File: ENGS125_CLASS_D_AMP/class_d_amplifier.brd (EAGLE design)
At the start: 100 x 80 mm, 24 parts, among them J1 BANANA_JACK_CT3151, J2 BANANA_JACK_CT3151, J3 BANANA_JACK_CT3151, J4 BANANA_JACK_CT3151, J5 BANANA_JACK_CT3151, J6 BANANA_JACK_CT3151, M1 BSC050NE2LSATMA1, M2 BSC050NE2LSATMA1, U1 LTC6992TSOT-23, U2 LTC4449

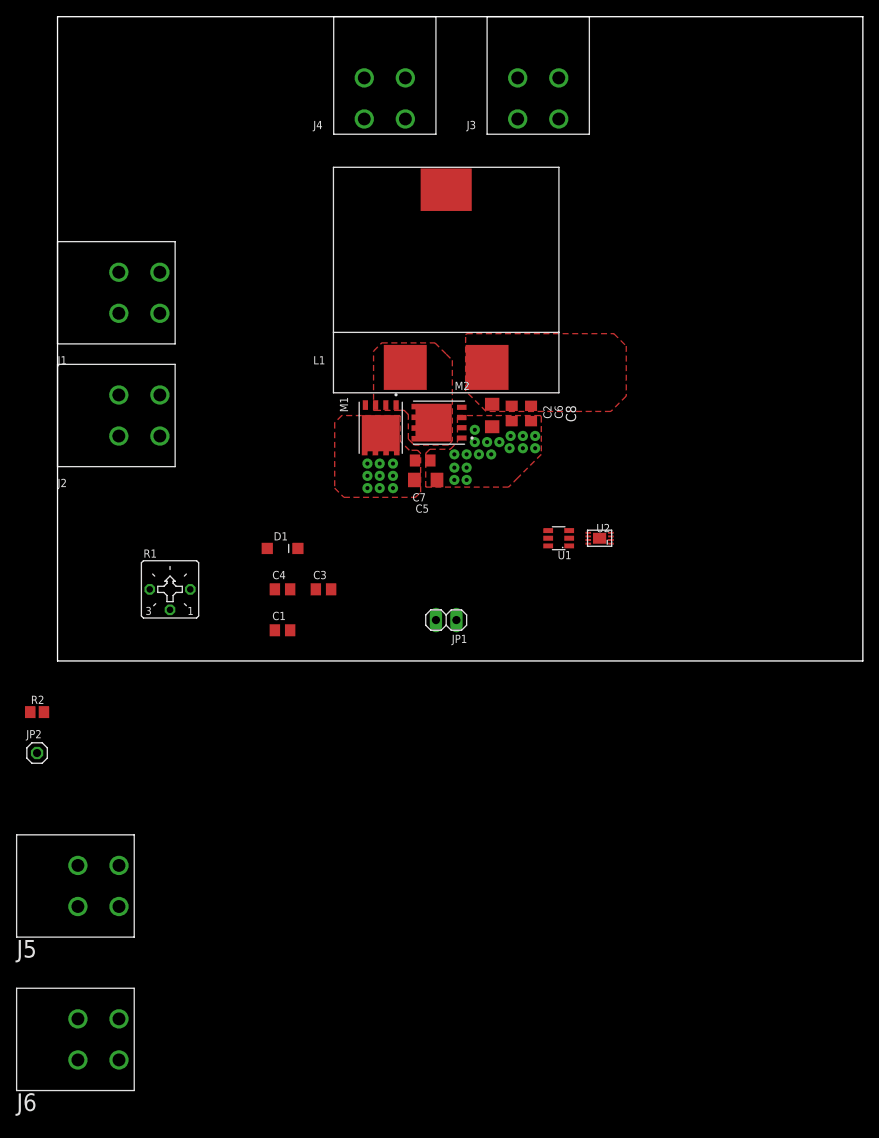
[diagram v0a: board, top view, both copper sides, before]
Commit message: Initial placement of banana jack connectors
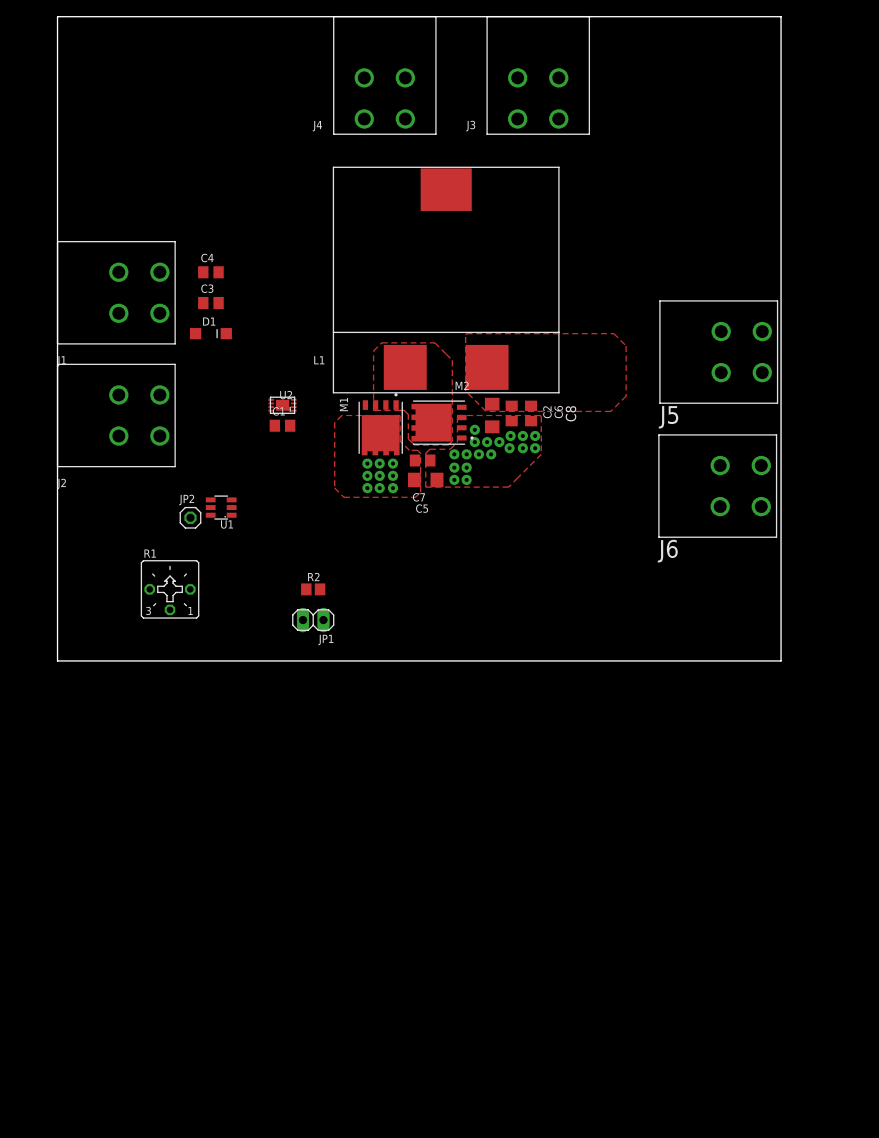
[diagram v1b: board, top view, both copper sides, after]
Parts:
- moved J6 105.3 mm to (84.8, 21.7)
- moved J5 103.8 mm to (85.0, 38.4)
- moved U2 42.7 mm to (27.9, 31.8)
- moved U1 42.1 mm to (20.3, 19.1)
- moved C4 40.4 mm to (19.1, 48.3)
- moved C3 38.2 mm to (19.1, 44.5)
- moved R2 37.5 mm to (31.8, 8.89)
- moved JP2 34.9 mm to (16.5, 17.8)
- moved D1 28.1 mm to (19.1, 40.6)
- moved C1 25.4 mm to (27.9, 29.2)
- moved JP1 16.5 mm to (31.8, 5.08)
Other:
- board size 100 x 80 mm -> 89.8 x 80 mm

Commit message: Generated bottom layer GND plane
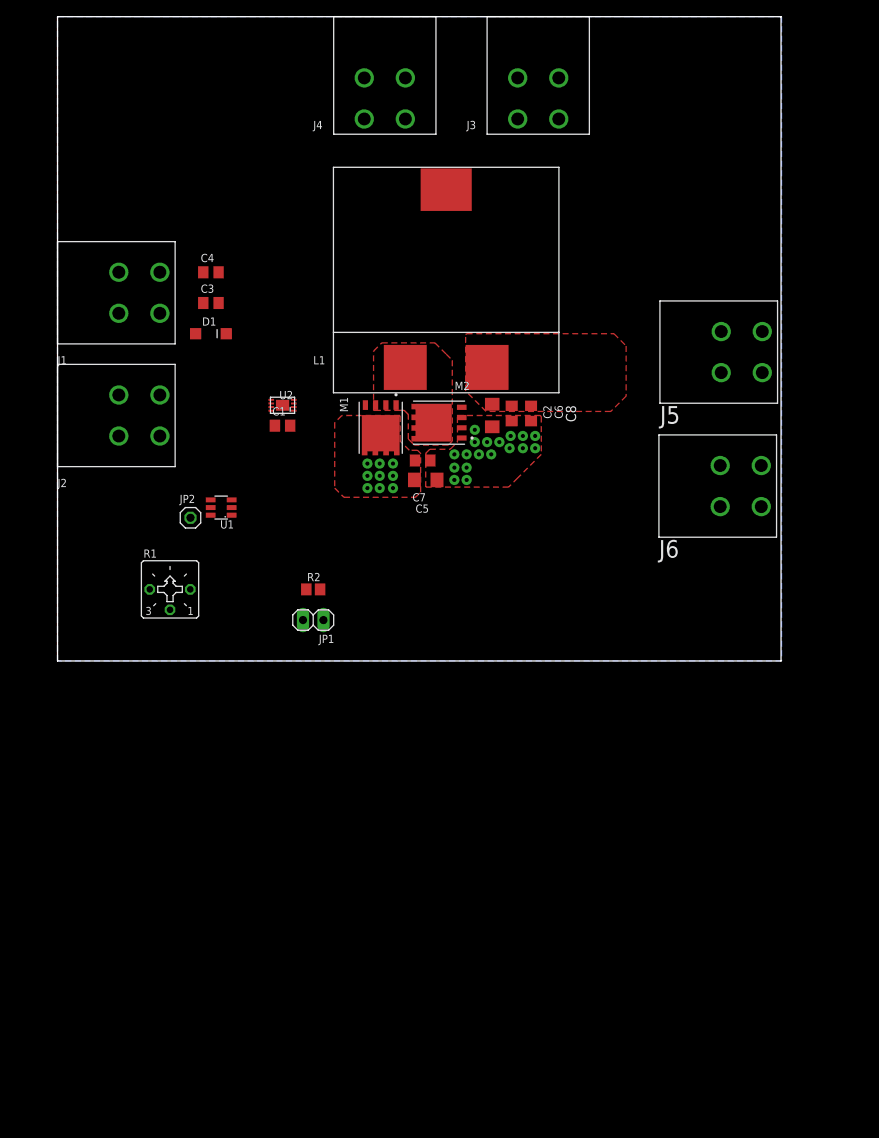
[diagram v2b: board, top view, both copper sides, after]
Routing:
- added copper zone on layer 16, net GND
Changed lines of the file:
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@@
 <layers>
 <layer number="1" name="Top" color="4" fill="1" visible="yes" active="yes"/>
-<layer number="2" name="Route2" color="1" fill="3" visible="no" active="yes"/>
+<layer number="2" name="Route2" color="1" fill="3" visible="yes" active="yes"/>
 <layer number="3" name="Route3" color="4" fill="3" visible="no" active="yes"/>
 <layer number="14" name="Route14" color="1" fill="6" visible="no" active="yes"/>
@@
 <vertex x="59.944" y="30.48"/>
 </polygon>
-<wire x1="43.19" y1="67.3" x2="43.19" y2="72.4" width="0" layer="19" extent="1-1"/>
-<wire x1="38.09" y1="72.4" x2="43.19" y2="72.4" width="0" layer="19" extent="1-1"/>
-<wire x1="38.09" y1="67.3" x2="43.19" y2="67.3" width="0" layer="19" extent="1-1"/>
-<wire x1="50.196" y1="30.226" x2="43.19" y2="67.3" width="0" layer="19" extent="1-1"/>
-<wire x1="19.02" y1="20" x2="59.309" y2="26.416" width="0" layer="19" extent="1-1"/>
+<polygon width="0.1524" layer="16">
+<vertex x="0" y="80.01"/>
+<vertex x="89.916" y="80.01"/>
+<vertex x="89.916" y="0"/>
+<vertex x="0" y="0"/>
+</polygon>
+<wire x1="20" y1="44.45" x2="20" y2="48.26" width="0" layer="19" extent="1-1"/>
+<wire x1="12.71" y1="33.03" x2="20" y2="44.45" width="0" layer="19" extent="1-1"/>
+<wire x1="30.9" y1="8.89" x2="30.48" y2="5.08" width="0" layer="19" extent="1-1"/>
+<wire x1="19.02" y1="20" x2="12.71" y2="27.93" width="0" layer="19" extent="1-1"/>
 <wire x1="27.94" y1="31.75" x2="19.02" y2="20" width="0" layer="19" extent="1-1"/>
 <wire x1="29.34" y1="32.425" x2="27.94" y2="31.75" width="0" layer="19" extent="1-1"/>
-<wire x1="33.02" y1="5.08" x2="19.02" y2="20" width="0" layer="19" extent="1-1"/>
-<wire x1="30.48" y1="5.08" x2="33.02" y2="5.08" width="0" layer="19" extent="1-1"/>
-<wire x1="20" y1="48.26" x2="30.48" y2="5.08" width="0" layer="19" extent="1-1"/>
-<wire x1="11.4554" y1="8.89" x2="20" y2="48.26" width="0" layer="19" extent="1-1"/>
-<wire x1="12.71" y1="27.93" x2="11.4554" y2="8.89" width="0" layer="19" extent="1-1"/>
-<wire x1="12.71" y1="33.03" x2="12.71" y2="27.93" width="0" layer="19" extent="1-1"/>
-<wire x1="7.61" y1="33.03" x2="12.71" y2="33.03" width="0" layer="19" extent="1-1"/>
-<wire x1="7.61" y1="27.93" x2="12.71" y2="27.93" width="0" layer="19" extent="1-1"/>
-<wire x1="30.9" y1="8.89" x2="20" y2="48.26" width="0" layer="19" extent="1-1"/>
-<wire x1="20" y1="44.45" x2="30.9" y2="8.89" width="0" layer="19" extent="1-1"/>
-<wire x1="82.286" y1="24.267" x2="20" y2="44.45" width="0" layer="19" extent="1-1"/>
-<wire x1="82.286" y1="19.167" x2="82.286" y2="24.267" width="0" layer="19" extent="1-1"/>
-<wire x1="87.386" y1="19.167" x2="82.286" y2="19.167" width="0" layer="19" extent="1-1"/>
-<wire x1="87.386" y1="24.267" x2="82.286" y2="24.267" width="0" layer="19" extent="1-1"/>
 </signal>
 <signal name="VGG">
@@
 <contactref element="J1" pad="P$2"/>
 <contactref element="U1" pad="5"/>
+<wire x1="18.1" y1="44.45" x2="18.1" y2="48.26" width="0" layer="19" extent="1-1"/>
+<wire x1="17.15" y1="40.64" x2="18.1" y2="44.45" width="0" layer="19" extent="1-1"/>
+<wire x1="12.71" y1="43.17" x2="17.15" y2="40.64" width="0" layer="19" extent="1-1"/>
+<wire x1="12.71" y1="48.27" x2="12.71" y2="43.17" width="0" layer="19" extent="1-1"/>
+<wire x1="7.61" y1="48.27" x2="12.71" y2="48.27" width="0" layer="19" extent="1-1"/>
+<wire x1="7.61" y1="43.17" x2="12.71" y2="43.17" width="0" layer="19" extent="1-1"/>
+<wire x1="26.54" y1="31.975" x2="17.15" y2="40.64" width="0" layer="19" extent="1-1"/>
 <wire x1="26.54" y1="31.525" x2="26.54" y2="31.975" width="0" layer="19" extent="1-1"/>
-<wire x1="19.02" y1="19.05" x2="26.54" y2="31.975" width="0" layer="19" extent="1-1"/>
-<wire x1="18.1" y1="48.26" x2="19.02" y2="19.05" width="0" layer="19" extent="1-1"/>
-<wire x1="17.15" y1="40.64" x2="18.1" y2="48.26" width="0" layer="19" extent="1-1"/>
-<wire x1="18.1" y1="44.45" x2="17.15" y2="40.64" width="0" layer="19" extent="1-1"/>
-<wire x1="7.61" y1="43.17" x2="17.15" y2="40.64" width="0" layer="19" extent="1-1"/>
-<wire x1="7.61" y1="48.27" x2="7.61" y2="43.17" width="0" layer="19" extent="1-1"/>
-<wire x1="12.71" y1="48.27" x2="7.61" y2="48.27" width="0" layer="19" extent="1-1"/>
-<wire x1="12.71" y1="43.17" x2="7.61" y2="43.17" width="0" layer="19" extent="1-1"/>
+<wire x1="19.02" y1="19.05" x2="26.54" y2="31.525" width="0" layer="19" extent="1-1"/>
 </signal>
 <signal name="VPWM">
@@
 <contactref element="U2" pad="8"/>
 <contactref element="C1" pad="1"/>
-<wire x1="20.95" y1="40.64" x2="26.54" y2="31.075" width="0" layer="19" extent="1-1"/>
-<wire x1="26.99" y1="29.21" x2="20.95" y2="40.64" width="0" layer="19" extent="1-1"/>
+<wire x1="26.54" y1="31.075" x2="20.95" y2="40.64" width="0" layer="19" extent="1-1"/>
+<wire x1="26.99" y1="29.21" x2="26.54" y2="31.075" width="0" layer="19" extent="1-1"/>
 </signal>
 <signal name="VSW">
@@
 <vertex x="39.243" y="31.115"/>
 </polygon>
-<wire x1="46.696" y1="29.591" x2="29.34" y2="31.525" width="0" layer="19" extent="1-1"/>
-<wire x1="28.89" y1="29.21" x2="44.196" y2="27.596" width="0" layer="19" extent="1-1"/>
+<wire x1="28.89" y1="29.21" x2="29.34" y2="31.525" width="0" layer="19" extent="1-1"/>
+<wire x1="39.497" y1="31.781" x2="29.34" y2="31.525" width="0" layer="19" extent="1-1"/>
 </signal>
 <signal name="VOUT">
@@
 <vertex x="53.213" y="30.988"/>
 </polygon>
-<wire x1="87.513" y1="35.804" x2="82.413" y2="35.804" width="0" layer="19" extent="1-1"/>
-<wire x1="82.413" y1="40.904" x2="82.413" y2="35.804" width="0" layer="19" extent="1-1"/>
-<wire x1="87.513" y1="40.904" x2="87.513" y2="35.804" width="0" layer="19" extent="1-1"/>
-<wire x1="53.975" y1="31.88" x2="87.513" y2="40.904" width="0" layer="19" extent="1-1"/>
+<wire x1="87.513" y1="35.804" x2="87.513" y2="40.904" width="0" layer="19" extent="1-1"/>
+<wire x1="82.413" y1="40.904" x2="87.513" y2="40.904" width="0" layer="19" extent="1-1"/>
+<wire x1="82.413" y1="35.804" x2="87.513" y2="35.804" width="0" layer="19" extent="1-1"/>
+<wire x1="58.801" y1="31.684" x2="82.413" y2="35.804" width="0" layer="19" extent="1-1"/>
 </signal>
 <signal name="VIN">
@@
 <contactref element="U2" pad="3"/>
 <contactref element="M2" pad="4"/>
-<wire x1="50.196" y1="31.496" x2="29.34" y2="31.975" width="0" layer="19" extent="1-1"/>
+<wire x1="29.34" y1="31.975" x2="50.196" y2="31.496" width="0" layer="19" extent="1-1"/>
 </signal>
 <signal name="TG">
 <contactref element="U2" pad="1"/>
 <contactref element="M1" pad="4"/>
-<wire x1="38.227" y1="31.781" x2="29.34" y2="31.075" width="0" layer="19" extent="1-1"/>
+<wire x1="29.34" y1="31.075" x2="38.227" y2="31.781" width="0" layer="19" extent="1-1"/>
 </signal>
 <signal name="N$3">

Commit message: Condensed board shape after replacement of connectors
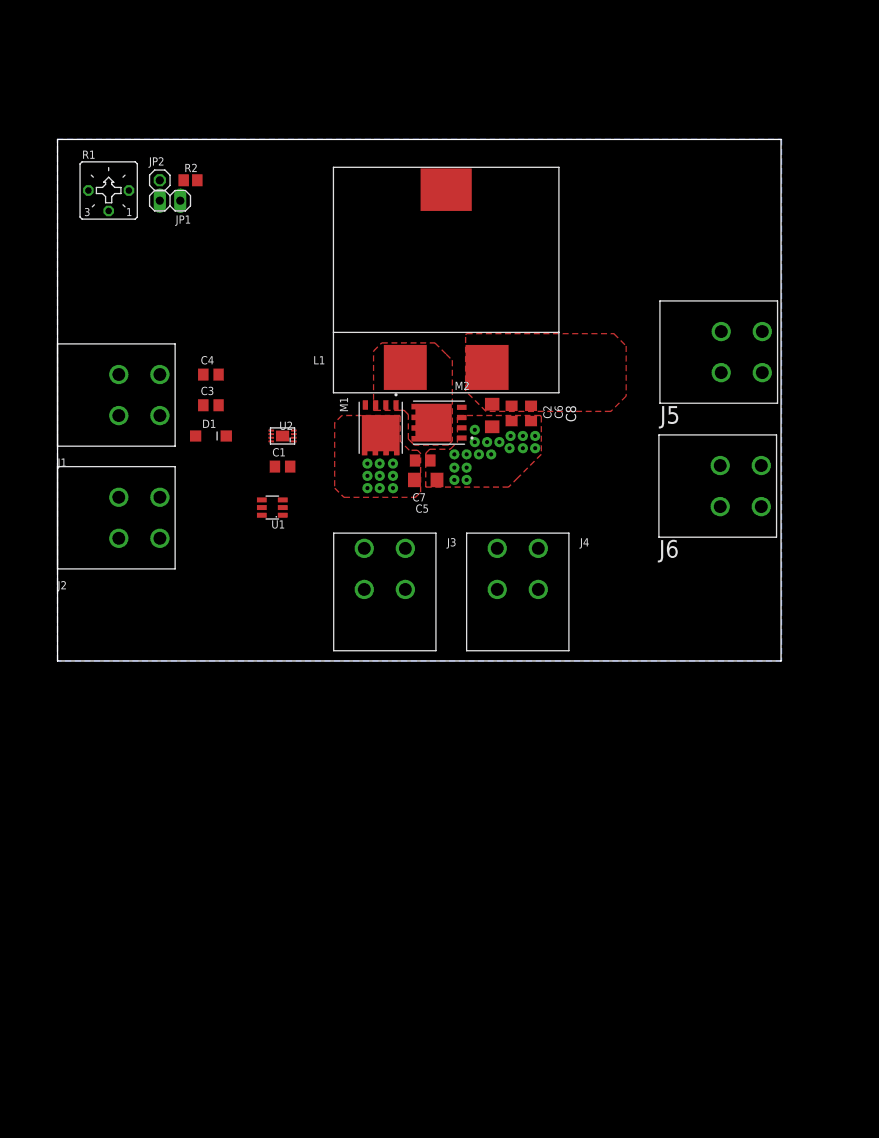
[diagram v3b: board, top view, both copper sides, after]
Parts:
- moved J3 61.4 mm to (40.6, 11.4), turned to 90 degrees
- moved J4 60.7 mm to (57.1, 11.4), turned to 90 degrees
- moved JP1 55.0 mm to (14.0, 57.1)
- moved R2 53.0 mm to (16.5, 59.7)
- moved R1 50.1 mm to (6.35, 58.4)
- moved JP2 42.1 mm to (12.7, 59.7)
- moved C3 12.7 mm to (19.1, 31.8)
- moved D1 12.7 mm to (19.1, 27.9)
- moved J2 12.7 mm to (10.2, 17.8)
- moved C4 12.7 mm to (19.1, 35.6)
- moved J1 12.7 mm to (10.2, 33.0)
- moved U1 6.35 mm to (26.7, 19.1)
- moved C1 5.08 mm to (27.9, 24.1)
- moved U2 3.81 mm to (27.9, 27.9)
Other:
- board size 89.8 x 80 mm -> 89.8 x 64.8 mm
